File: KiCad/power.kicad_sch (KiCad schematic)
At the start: 0 parts

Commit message: kian made som changes to the scmatices for power an added a libaery called power componentes
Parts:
- added BT1: Battery, symbol Device:Battery
- added C1, C2: 10uf, symbol Device:C
- added D1: LED Green, symbol Device:LED
- added D2: LED RED, symbol Device:LED
- added R2, R3: 1k, symbol Device:R
- added R4: 1.2k, symbol Device:R
- added U2: ~, symbol New_Library:C404969
- added U3: ~, symbol Power comonentes:TP4056
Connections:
- new net: D2.1 (K), R3.2
- new net: C1.1, D1.2 (A), D2.2 (A), U2.1 (VBUS), U3.4 (Vcc), U3.8 (CE)
- new net: D1.1 (K), R2.1
- new net: R2.2, U3. (STDBY#)
- new net: BT1.1 (+), C2.1, U3.5 (BAT)
- new net: R4.1, U3.2 (PROG)
- new net: R3.1, U3.7 (CHRG)
- new net GND: BT1.2 (-), C1.2, C2.2, R4.2, U2.5 (GND), U3.1 (TEMP), U3.3 (GND)
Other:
- note added: "Battery charger"
- note added: "USB"

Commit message: kian made som changes to the scmatices
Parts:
- added R5: 1k, symbol Device:R
- added U4: ~, symbol Power comonentes:C150742_(LDO/_UVLO)
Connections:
- net GND: now also U4.2 (GND)
- new net: R5.1, U4.1 (VIN)
- new net: R5.2, U4.3 (EN)
- new net 3.3 V: U4.5 (VOUT)
- no-connect marks 0 -> 1
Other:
- note added: "polarity protector and 3.3 volt regulater"
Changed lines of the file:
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@@
   (junction (at 63.5 30.48) (diameter 0) (color 0 0 0 0)
   )
+  (no_connect (at 229.87 41.91))
   (wire (pts (xy 44.45 41.91) (xy 45.72 41.91))
     (stroke (width 0) (type default))
@@
     (stroke (width 0) (type default))
   )
+  (wire (pts (xy 195.58 34.29) (xy 201.93 34.29))
+    (stroke (width 0) (type default))
+  )
   (wire (pts (xy 53.34 30.48) (xy 63.5 30.48))
     (stroke (width 0) (type default))
   )
+  (wire (pts (xy 195.58 42.545) (xy 201.93 42.545))
+    (stroke (width 0) (type default))
+  )
   (wire (pts (xy 137.16 30.48) (xy 137.16 31.75))
     (stroke (width 0) (type default))
@@
     (stroke (width 0) (type default))
   )
+  (wire (pts (xy 201.93 42.545) (xy 201.93 41.91))
+    (stroke (width 0) (type default))
+  )
   (wire (pts (xy 109.22 30.48) (xy 125.73 30.48))
     (stroke (width 0) (type default))
@@
     (stroke (width 0) (type default))
   )
+  (wire (pts (xy 195.58 34.925) (xy 195.58 34.29))
+    (stroke (width 0) (type default))
+  )
   (wire (pts (xy 85.09 34.29) (xy 85.09 30.48))
     (stroke (width 0) (type default))
@@
     (stroke (width 0) (type default))
   )
+  (wire (pts (xy 200.66 38.1) (xy 201.93 38.1))
+    (stroke (width 0) (type default))
+  )
   (wire (pts (xy 85.09 30.48) (xy 90.17 30.48))
     (stroke (width 0) (type default))
@@
     (stroke (width 0) (type default))
   )
+  (wire (pts (xy 200.66 38.1) (xy 200.66 46.99))
+    (stroke (width 0) (type default))
+  )
   (wire (pts (xy 88.265 41.91) (xy 90.17 41.91))
     (stroke (width 0) (type default))
@@
     (stroke (width 0) (type default))
   )
+  (rectangle (start 134.62 20.955) (end 149.86 62.23)
+    (stroke (width 0) (type default))
+    (fill (type none))
+  )
   (rectangle (start 50.8 20.955) (end 134.62 62.23)
     (stroke (width 0) (type default))
     (fill (type none))
   )
+  (rectangle (start 149.86 20.955) (end 184.785 62.23)
+    (stroke (width 0) (type default))
+    (fill (type none))
+  )
   (rectangle (start 23.495 20.955) (end 50.8 61.595)
+    (stroke (width 0) (type default))
+    (fill (type none))
+  )
+  (rectangle (start 184.785 20.955) (end 250.825 62.23)
     (stroke (width 0) (type default))
     (fill (type none))
@@
   )
   (text "USB" (at 26.035 60.325 0)
+    (effects (font (size 1.27 1.27)) (justify left bottom))
+  )
+  (text "polarity protector and 3.3 volt regulater" (at 186.69 60.96 0)
+    (effects (font (size 1.27 1.27)) (justify left bottom))
+  )
+  (label "3.3 V" (at 229.87 35.56 0) (fields_autoplaced)
     (effects (font (size 1.27 1.27)) (justify left bottom))
   )
@@
         )
       )
+      (project "power"
+        (path "/d9c34bc1-cf5e-42ef-a2b2-2cfbae723006"
+          (reference "D2") (unit 1)
+        )
+      )
       (project "tep work"
         (path "/dbd26d19-6d63-47f2-b172-340d78bc82ae"
@@
         )
       )
-      (project "tep work"
-        (path "/dbd26d19-6d63-47f2-b172-340d78bc82ae"
+      (project "power"
+        (path "/d9c34bc1-cf5e-42ef-a2b2-2cfbae723006"
           (reference "#PWR07") (unit 1)
         )
       )
+      (project "tep work"
+        (path "/dbd26d19-6d63-47f2-b172-340d78bc82ae"
+          (reference "#PWR07") (unit 1)
+        )
+      )
     )
   )
@@
         )
       )
+      (project "power"
+        (path "/d9c34bc1-cf5e-42ef-a2b2-2cfbae723006"
+          (reference "#PWR013") (unit 1)
+        )
+      )
       (project "tep work"
         (path "/dbd26d19-6d63-47f2-b172-340d78bc82ae"
@@
         )
       )
+      (project "power"
+        (path "/d9c34bc1-cf5e-42ef-a2b2-2cfbae723006"
+          (reference "#PWR08") (unit 1)
+        )
+      )
       (project "tep work"
         (path "/dbd26d19-6d63-47f2-b172-340d78bc82ae"
@@
       (project "EEE3088F_CKR"
         (path "/31e5d740-f3fb-4029-be8d-dfdc4f653d72/d53a003e-af2e-46c6-8ee9-c5701cef8adb"
+          (reference "#PWR011") (unit 1)
+        )
+      )
+      (project "power"
+        (path "/d9c34bc1-cf5e-42ef-a2b2-2cfbae723006"
           (reference "#PWR011") (unit 1)
         )
@@
         )
       )
+      (project "power"
+        (path "/d9c34bc1-cf5e-42ef-a2b2-2cfbae723006"
+          (reference "D1") (unit 1)
+        )
+      )
       (project "tep work"
         (path "/dbd26d19-6d63-47f2-b172-340d78bc82ae"
@@
       (project "EEE3088F_CKR"
         (path "/31e5d740-f3fb-4029-be8d-dfdc4f653d72/d53a003e-af2e-46c6-8ee9-c5701cef8adb"
+          (reference "R2") (unit 1)
+        )
+      )
+      (project "power"
+        (path "/d9c34bc1-cf5e-42ef-a2b2-2cfbae723006"
           (reference "R2") (unit 1)
         )
@@
         )
       )
+      (project "power"
+        (path "/d9c34bc1-cf5e-42ef-a2b2-2cfbae723006"
+          (reference "U2") (unit 1)
+        )
+      )
       (project "tep work"
         (path "/dbd26d19-6d63-47f2-b172-340d78bc82ae"
@@
         )
       )
-      (project "tep work"
-        (path "/dbd26d19-6d63-47f2-b172-340d78bc82ae"
+      (project "power"
+        (path "/d9c34bc1-cf5e-42ef-a2b2-2cfbae723006"
           (reference "C2") (unit 1)
         )
       )
+      (project "tep work"
+        (path "/dbd26d19-6d63-47f2-b172-340d78bc82ae"
+          (reference "C2") (unit 1)
+        )
+      )
+    )
+  )
+  (symbol (lib_id "power:GND") (at 200.66 46.99 0) (unit 1)
+    (in_bom yes) (on_board yes) (dnp no) (fields_autoplaced)
+    (property "Reference" "#PWR014" (at 200.66 53.34 0)
+      (effects (font (size 1.27 1.27)) hide)
+    )
+    (property "Value" "GND" (at 200.66 51.435 0)
+      (effects (font (size 1.27 1.27)))
+    )
+    (property "Footprint" "" (at 200.66 46.99 0)
+      (effects (font (size 1.27 1.27)) hide)
+    )
+    (property "Datasheet" "" (at 200.66 46.99 0)
+      (effects (font (size 1.27 1.27)) hide)
+    )
+    (pin "1")
+    (instances
+      (project "EEE3088F_CKR"
+        (path "/31e5d740-f3fb-4029-be8d-dfdc4f653d72/d53a003e-af2e-46c6-8ee9-c5701cef8adb"
+          (reference "#PWR014") (unit 1)
+        )
+      )
     )
   )
@@
         )
       )
+      (project "power"
+        (path "/d9c34bc1-cf5e-42ef-a2b2-2cfbae723006"
+          (reference "#PWR09") (unit 1)
+        )
+      )
       (project "tep work"
         (path "/dbd26d19-6d63-47f2-b172-340d78bc82ae"
@@
         )
       )
+      (project "power"
+        (path "/d9c34bc1-cf5e-42ef-a2b2-2cfbae723006"
+          (reference "#PWR010") (unit 1)
+        )
+      )
       (project "tep work"
         (path "/dbd26d19-6d63-47f2-b172-340d78bc82ae"
@@
         )
       )
+      (project "power"
+        (path "/d9c34bc1-cf5e-42ef-a2b2-2cfbae723006"
+          (reference "#PWR012") (unit 1)
+        )
+      )
       (project "tep work"
         (path "/dbd26d19-6d63-47f2-b172-340d78bc82ae"
@@
     )
   )
+  (symbol (lib_id "Device:R") (at 195.58 38.735 0) (unit 1)
+    (in_bom yes) (on_board yes) (dnp no) (fields_autoplaced)
+    (property "Reference" "R5" (at 197.485 38.1 0)
+      (effects (font (size 1.27 1.27)) (justify left))
+    )
+    (property "Value" "1k" (at 197.485 40.64 0)
+      (effects (font (size 1.27 1.27)) (justify left))
+    )
+    (property "Footprint" "" (at 193.802 38.735 90)
+      (effects (font (size 1.27 1.27)) hide)
+    )
+    (property "Datasheet" "~" (at 195.58 38.735 0)
+      (effects (font (size 1.27 1.27)) hide)
+    )
+    (pin "1")
+    (pin "2")
+    (instances
+      (project "EEE3088F_CKR"
+        (path "/31e5d740-f3fb-4029-be8d-dfdc4f653d72/d53a003e-af2e-46c6-8ee9-c5701cef8adb"
+          (reference "R5") (unit 1)
+        )
+      )
+    )
+  )
   (symbol (lib_id "Device:R") (at 112.395 47.625 0) (unit 1)
     (in_bom yes) (on_board yes) (dnp no) (fields_autoplaced)
@@
         )
       )
+      (project "power"
+        (path "/d9c34bc1-cf5e-42ef-a2b2-2cfbae723006"
+          (reference "R4") (unit 1)
+        )
+      )
       (project "tep work"
         (path "/dbd26d19-6d63-47f2-b172-340d78bc82ae"
@@
       (project "EEE3088F_CKR"
         (path "/31e5d740-f3fb-4029-be8d-dfdc4f653d72/d53a003e-af2e-46c6-8ee9-c5701cef8adb"
+          (reference "BT1") (unit 1)
+        )
+      )
+      (project "power"
+        (path "/d9c34bc1-cf5e-42ef-a2b2-2cfbae723006"
           (reference "BT1") (unit 1)
         )
@@
       (project "EEE3088F_CKR"
         (path "/31e5d740-f3fb-4029-be8d-dfdc4f653d72/d53a003e-af2e-46c6-8ee9-c5701cef8adb"
+          (reference "R3") (unit 1)
+        )
+      )
+      (project "power"
+        (path "/d9c34bc1-cf5e-42ef-a2b2-2cfbae723006"
           (reference "R3") (unit 1)
         )
@@
       (project "EEE3088F_CKR"
         (path "/31e5d740-f3fb-4029-be8d-dfdc4f653d72/d53a003e-af2e-46c6-8ee9-c5701cef8adb"
+          (reference "C1") (unit 1)
+        )
+      )
+      (project "power"
+        (path "/d9c34bc1-cf5e-42ef-a2b2-2cfbae723006"
           (reference "C1") (unit 1)
         )
@@
         )
       )
+      (project "power"
+        (path "/d9c34bc1-cf5e-42ef-a2b2-2cfbae723006"
+          (reference "U3") (unit 1)
+        )
+      )
       (project "tep work"
         (path "/dbd26d19-6d63-47f2-b172-340d78bc82ae"
@@
     )
   )
+  (symbol (lib_id "Power comonentes:C150742_(LDO/_UVLO)") (at 215.9 35.56 0) (unit 1)
+    (in_bom yes) (on_board yes) (dnp no) (fields_autoplaced)
+    (property "Reference" "U4" (at 215.5014 30.48 0)
+      (effects (font (size 1.27 1.27)))
+    )
+    (property "Value" "~" (at 215.9 35.56 0)
+      (effects (font (size 1.27 1.27)))
+    )
+    (property "Footprint" "" (at 215.9 35.56 0)
+      (effects (font (size 1.27 1.27)) hide)
+    )
+    (property "Datasheet" "" (at 215.9 35.56 0)
+      (effects (font (size 1.27 1.27)) hide)
+    )
+    (pin "1")
+    (pin "2")
+    (pin "3")
+    (pin "4")
+    (pin "5")
+    (instances
+      (project "EEE3088F_CKR"
+        (path "/31e5d740-f3fb-4029-be8d-dfdc4f653d72/d53a003e-af2e-46c6-8ee9-c5701cef8adb"
+          (reference "U4") (unit 1)
+        )
+      )
+    )
+  )
+  (sheet_instances
+    (path "/" (page "1"))
+  )
 )

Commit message: finale scamatic for today
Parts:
- removed U4: ~, symbol Power comonentes:C150742_(LDO/_UVLO)
- added C3, C4: 10f, symbol Device:C
- added U4: ~, symbol power_components_library:LM2937L-33-TQ2-R
- added U5: ~, symbol power_components_library:SI2301CDS-T1-GE3
- R5: value 1k -> R
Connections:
- net GND: now also C3.2, C4.2, U4.2 (GND), U4.4 (PAD)
- net at BT1.1 (+), C2.1, U3.5 (BAT): now also U5.D (3)
- net at R5.1: now also U5.gate (1)
- new net: C4.1, U4.1 (VIN), U5.s (2)
- new net 3.3 0ut: C3.1, U4.3 (VOUT)
- no-connect marks 1 -> 0
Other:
- note added: "UVLO and 3.3 volt regulater"
- note removed: "polarity protector and 3.3 volt regulater"

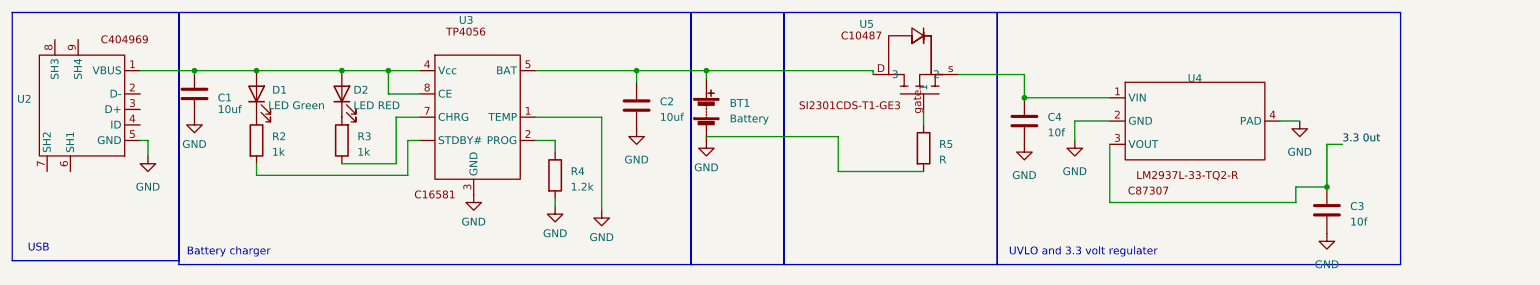
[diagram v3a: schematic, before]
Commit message: Q1.2 done
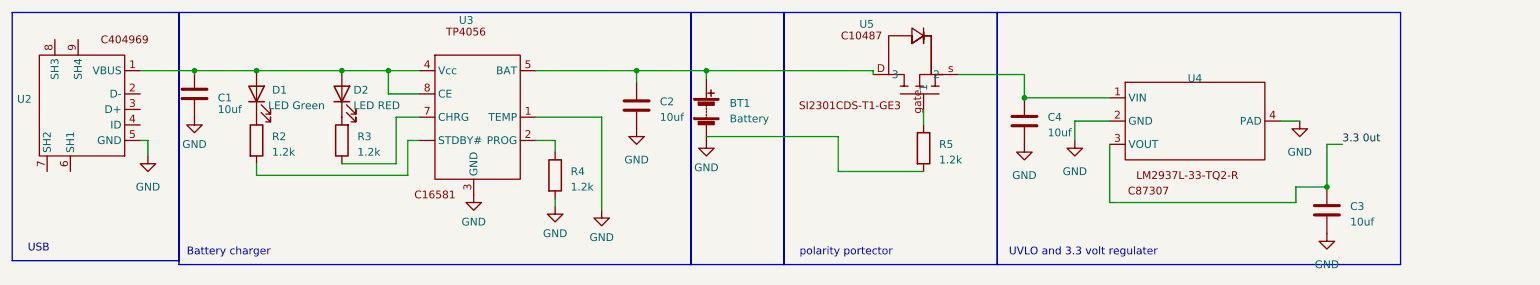
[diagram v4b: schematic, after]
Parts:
- C3, C4: value 10f -> 10uf
- R2, R3: value 1k -> 1.2k
- R5: value R -> 1.2k
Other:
- note added: "polarity portector"
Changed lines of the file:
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@@
     (fill (type none))
+  )
+  (text "polarity portector" (at 152.4 60.96 0)
+    (effects (font (size 1.27 1.27)) (justify left bottom))
   )
   (text "Battery charger " (at 52.07 60.96 0)
@@
       (effects (font (size 1.27 1.27)) (justify left))
     )
-    (property "Value" "R" (at 175.26 45.085 0)
+    (property "Value" "1.2k" (at 175.26 45.085 0)
       (effects (font (size 1.27 1.27)) (justify left))
     )
@@
       (project "EEE3088F_CKR"
         (path "/31e5d740-f3fb-4029-be8d-dfdc4f653d72/d53a003e-af2e-46c6-8ee9-c5701cef8adb"
+          (reference "R5") (unit 1)
+        )
+      )
+      (project "power"
+        (path "/d9c34bc1-cf5e-42ef-a2b2-2cfbae723006"
           (reference "R5") (unit 1)
         )
@@
       (effects (font (size 1.27 1.27)) (justify left))
     )
-    (property "Value" "1k" (at 66.04 43.815 0)
+    (property "Value" "1.2k" (at 66.04 43.815 0)
       (effects (font (size 1.27 1.27)) (justify left))
     )
@@
       (project "EEE3088F_CKR"
         (path "/31e5d740-f3fb-4029-be8d-dfdc4f653d72/d53a003e-af2e-46c6-8ee9-c5701cef8adb"
+          (reference "#PWR015") (unit 1)
+        )
+      )
+      (project "power"
+        (path "/d9c34bc1-cf5e-42ef-a2b2-2cfbae723006"
           (reference "#PWR015") (unit 1)
         )
@@
         )
       )
+      (project "power"
+        (path "/d9c34bc1-cf5e-42ef-a2b2-2cfbae723006"
+          (reference "U5") (unit 1)
+        )
+      )
     )
   )
@@
       (project "EEE3088F_CKR"
         (path "/31e5d740-f3fb-4029-be8d-dfdc4f653d72/d53a003e-af2e-46c6-8ee9-c5701cef8adb"
+          (reference "#PWR016") (unit 1)
+        )
+      )
+      (project "power"
+        (path "/d9c34bc1-cf5e-42ef-a2b2-2cfbae723006"
           (reference "#PWR016") (unit 1)
         )
@@
         )
       )
+      (project "power"
+        (path "/d9c34bc1-cf5e-42ef-a2b2-2cfbae723006"
+          (reference "U4") (unit 1)
+        )
+      )
     )
   )
@@
         )
       )
+      (project "power"
+        (path "/d9c34bc1-cf5e-42ef-a2b2-2cfbae723006"
+          (reference "#PWR017") (unit 1)
+        )
+      )
     )
   )
@@
       (effects (font (size 1.27 1.27)) (justify left))
     )
-    (property "Value" "10f" (at 242.57 55.245 0)
+    (property "Value" "10uf" (at 242.57 55.245 0)
       (effects (font (size 1.27 1.27)) (justify left))
     )
@@
       (project "EEE3088F_CKR"
         (path "/31e5d740-f3fb-4029-be8d-dfdc4f653d72/d53a003e-af2e-46c6-8ee9-c5701cef8adb"
+          (reference "C3") (unit 1)
+        )
+      )
+      (project "power"
+        (path "/d9c34bc1-cf5e-42ef-a2b2-2cfbae723006"
           (reference "C3") (unit 1)
         )
@@
       (effects (font (size 1.27 1.27)) (justify right))
     )
-    (property "Value" "1k" (at 80.01 43.815 0)
+    (property "Value" "1.2k" (at 80.01 43.815 0)
       (effects (font (size 1.27 1.27)) (justify right))
     )
@@
       (effects (font (size 1.27 1.27)) (justify left))
     )
-    (property "Value" "10f" (at 193.04 40.64 0)
+    (property "Value" "10uf" (at 193.04 40.64 0)
       (effects (font (size 1.27 1.27)) (justify left))
     )
@@
       (project "EEE3088F_CKR"
         (path "/31e5d740-f3fb-4029-be8d-dfdc4f653d72/d53a003e-af2e-46c6-8ee9-c5701cef8adb"
+          (reference "C4") (unit 1)
+        )
+      )
+      (project "power"
+        (path "/d9c34bc1-cf5e-42ef-a2b2-2cfbae723006"
           (reference "C4") (unit 1)
         )
@@
           (reference "#PWR014") (unit 1)
         )
+      )
+      (project "power"
+        (path "/d9c34bc1-cf5e-42ef-a2b2-2cfbae723006"
+          (reference "#PWR014") (unit 1)
+        )

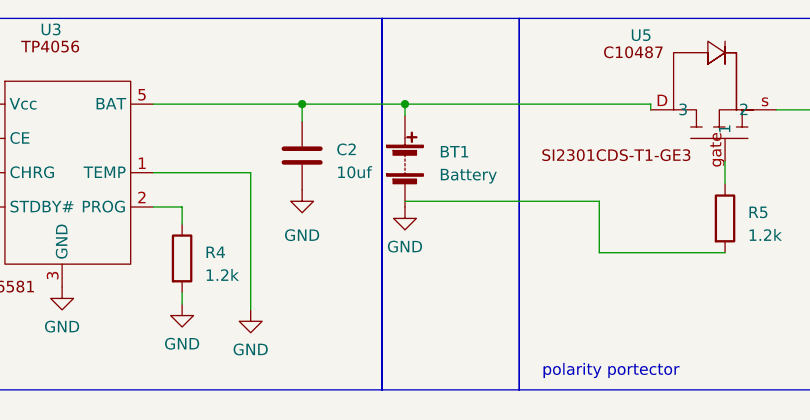
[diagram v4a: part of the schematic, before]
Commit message: changed battery to DNP
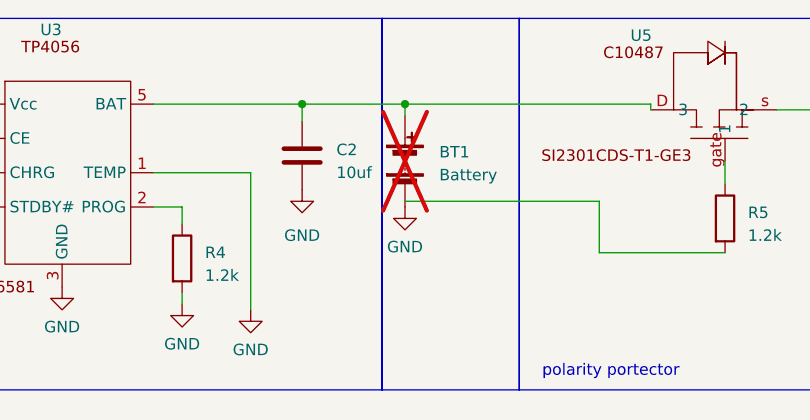
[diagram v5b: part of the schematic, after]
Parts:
- BT1: now not fitted
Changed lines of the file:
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@@
   )
   (symbol (lib_id "Device:Battery") (at 137.16 36.83 0) (unit 1)
-    (in_bom yes) (on_board yes) (dnp no) (fields_autoplaced)
+    (in_bom yes) (on_board yes) (dnp yes) (fields_autoplaced)
     (property "Reference" "BT1" (at 140.97 35.814 0)
       (effects (font (size 1.27 1.27)) (justify left))
